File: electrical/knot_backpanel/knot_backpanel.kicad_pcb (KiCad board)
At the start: 2 copper layers, 61 x 13 mm, 0 parts

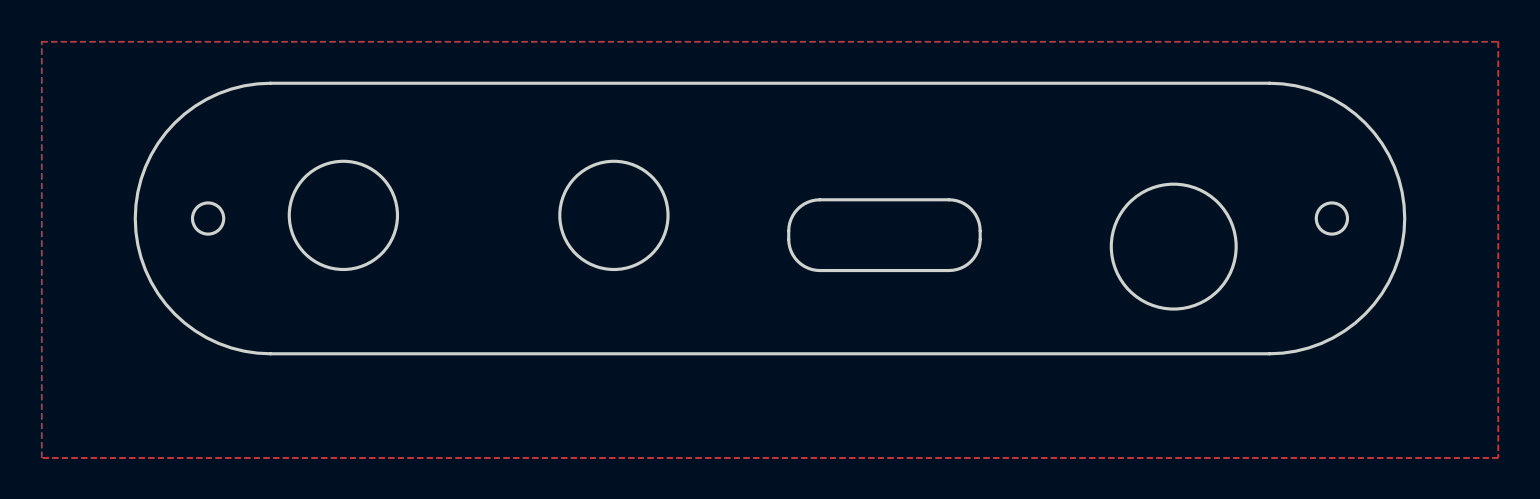
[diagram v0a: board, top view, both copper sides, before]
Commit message: SUKU sync + fw connect status led function added
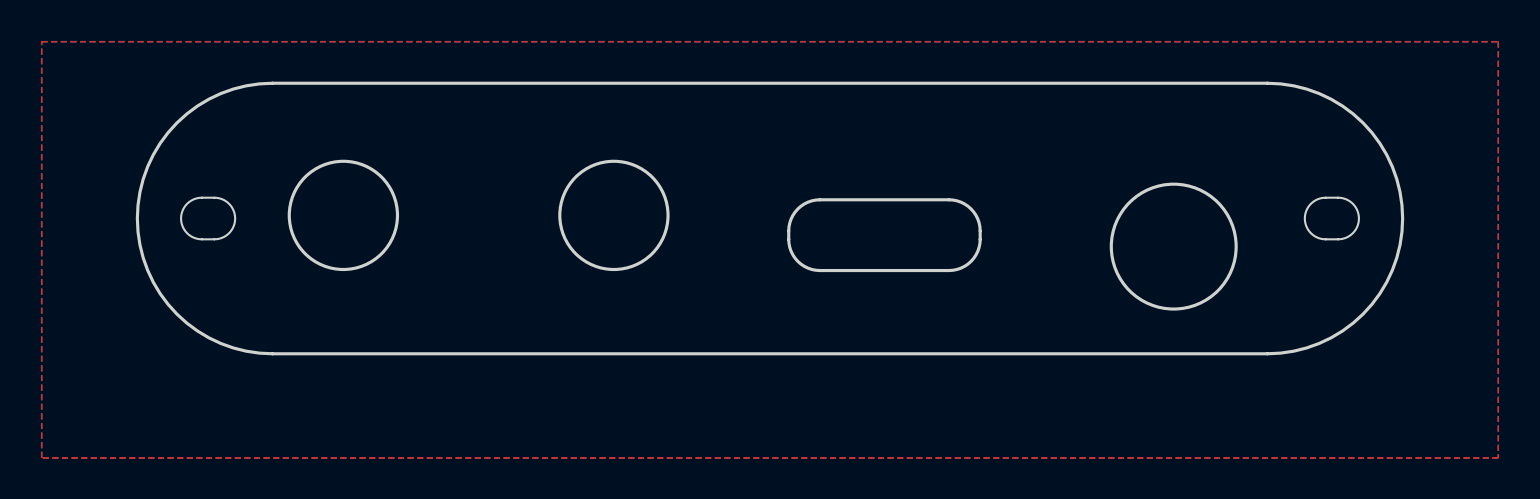
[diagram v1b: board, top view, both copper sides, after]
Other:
- board size 61 x 13 mm -> 60.8 x 13 mm
- board text added: "Backpanel Inside 2022/10"
- board text removed: "Backpanel Inside 2022/9"
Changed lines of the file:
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@@
   )
   (net 0 "")
+  (gr_arc (start 127.3 92.5) (mid 128.3 93.5) (end 127.3 94.5) (layer "Edge.Cuts") (width 0.1))
   (gr_circle (center 79.5 93.35) (end 82.1 93.35) (layer "Edge.Cuts") (width 0.15) (fill none))
-  (gr_line (start 76 100) (end 124 100) (layer "Edge.Cuts") (width 0.15))
+  (gr_line (start 76.1 100) (end 123.9 100) (layer "Edge.Cuts") (width 0.15))
   (gr_line (start 100.9 94.1) (end 100.9 94.5) (layer "Edge.Cuts") (width 0.15))
+  (gr_line (start 72.7 94.5) (end 73.3 94.5) (layer "Edge.Cuts") (width 0.1))
   (gr_line (start 108.6 92.6) (end 102.4 92.6) (layer "Edge.Cuts") (width 0.15))
   (gr_arc (start 110.1 94.5) (mid 109.66066 95.56066) (end 108.6 96) (layer "Edge.Cuts") (width 0.15))
+  (gr_line (start 126.7 94.5) (end 127.3 94.5) (layer "Edge.Cuts") (width 0.1))
   (gr_arc (start 102.4 96) (mid 101.33934 95.56066) (end 100.9 94.5) (layer "Edge.Cuts") (width 0.15))
   (gr_line (start 108.6 96) (end 102.4 96) (layer "Edge.Cuts") (width 0.15))
-  (gr_arc (start 124 87) (mid 130.5 93.5) (end 124 100) (layer "Edge.Cuts") (width 0.15))
-  (gr_arc (start 76 100) (mid 69.5 93.5) (end 76 87) (layer "Edge.Cuts") (width 0.15))
+  (gr_arc (start 123.9 87) (mid 130.4 93.5) (end 123.9 100) (layer "Edge.Cuts") (width 0.15))
+  (gr_arc (start 76.1 100) (mid 69.6 93.5) (end 76.1 87) (layer "Edge.Cuts") (width 0.15))
   (gr_arc (start 108.6 92.6) (mid 109.66066 93.03934) (end 110.1 94.1) (layer "Edge.Cuts") (width 0.15))
+  (gr_arc (start 126.7 94.5) (mid 125.7 93.5) (end 126.7 92.5) (layer "Edge.Cuts") (width 0.1))
+  (gr_arc (start 72.7 94.5) (mid 71.7 93.5) (end 72.7 92.5) (layer "Edge.Cuts") (width 0.1))
+  (gr_line (start 72.7 92.5) (end 73.3 92.5) (layer "Edge.Cuts") (width 0.1))
   (gr_circle (center 92.5 93.35) (end 95.1 93.35) (layer "Edge.Cuts") (width 0.15) (fill none))
   (gr_arc (start 100.9 94.1) (mid 101.33934 93.03934) (end 102.4 92.6) (layer "Edge.Cuts") (width 0.15))
   (gr_circle (center 119.4 94.85) (end 122.4 94.85) (layer "Edge.Cuts") (width 0.15) (fill none))
   (gr_line (start 110.1 94.1) (end 110.1 94.5) (layer "Edge.Cuts") (width 0.15))
-  (gr_line (start 76 87) (end 124 87) (layer "Edge.Cuts") (width 0.15))
-  (gr_circle (center 73 93.5) (end 73.75 93.5) (layer "Edge.Cuts") (width 0.15) (fill none))
-  (gr_circle (center 127 93.5) (end 127.75 93.5) (layer "Edge.Cuts") (width 0.15) (fill none))
-  (gr_text "Backpanel Inside 2022/9" (at 100 89) (layer "B.SilkS")
+  (gr_line (start 76.1 87) (end 123.9 87) (layer "Edge.Cuts") (width 0.15))
+  (gr_line (start 126.7 92.5) (end 127.3 92.5) (layer "Edge.Cuts") (width 0.1))
+  (gr_arc (start 73.3 92.5) (mid 74.3 93.5) (end 73.3 94.5) (layer "Edge.Cuts") (width 0.1))
+  (gr_text "Backpanel Inside 2022/10" (at 100 89) (layer "B.SilkS")
     (effects (font (size 1.5 1.5) (thickness 0.3)) (justify mirror))
   )
